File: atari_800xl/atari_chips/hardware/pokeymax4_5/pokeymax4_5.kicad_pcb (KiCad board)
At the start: 4 copper layers, 20.8 x 51.3 mm, 70 parts, among them J1 Conn_02x03_Odd_Even, J2 Conn_01x14_Pin, U2 TSV854IQ4T, U3 SN74CB3T16211DGVR, U5 SN74CB3T16211DGVR, Y1 ASE-49.152MHz

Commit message: Added pokeymax 4.54 (not yet made)
git-svn-id: svn+ssh://192.168.0.3/home/svnfpga/repo/trunk@1559 d6161ac3-aae1-4d52-9b05-ea9ac36b53d3
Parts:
- added C28: 220pF C0G, Capacitor_SMD:C_0402_1005Metric, F.Cu at (31.9, 30.6)
- added C29: 220pF C0G, Capacitor_SMD:C_0402_1005Metric, F.Cu at (25.6, 31.1)
- added R32: 31k6, Resistor_SMD:R_0402_1005Metric, F.Cu at (21.7, 29.3)
- added R33: 31k6, Resistor_SMD:R_0402_1005Metric, F.Cu at (30.6, 29.2)
- C13, C14: value 220pf C0G -> 220pF C0G
- R11, R13: value 560 -> 31k6
- R20, R21: value 33 -> 270
- moved C13 10.5 mm to (21.7, 28.3), turned to 180 degrees
- moved C14 4.54 mm to (29.6, 29.2), turned to 90 degrees
- moved R11 1.49 mm to (31.7, 29.2), turned to 90 degrees
- moved C9 0.94 mm to (32.5, 27.8)
- moved R12 0.63 mm to (32.7, 29.2), turned to 90 degrees
- moved R10 0.60 mm to (32.1, 26.8)
- moved C8 0.54 mm to (30.1, 27.8), turned to 180 degrees
- moved C10 0.53 mm to (23.7, 28.5), turned to 0 degrees
- moved R8 0.45 mm to (30.1, 26.8), turned to 180 degrees
- moved R14 0.40 mm to (30.0, 30.6)
- moved R15 0.26 mm to (21.9, 31.2)
- moved C12 0.21 mm to (21.7, 30.3)
- moved R16 0.19 mm to (23.7, 31.3)
- moved R13 0.06 mm to (23.6, 30.2), turned to 0 degrees
- moved C5 0.05 mm to (30.9, 24.9)
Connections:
- net Net-(J1-Pin_6) renamed /FPGA/TDO
- C12 pad 1: Net-(U2-IN2+) -> Net-(C12-Pad1)
- C13 pad 1: Net-(U2-OUT3) -> Net-(U2-IN2+)
- C13 pad 2: Net-(U2-IN3-) -> GND
- C14 pad 1: Net-(U2-OUT2) -> Net-(U2-IN3+)
- C14 pad 2: Net-(U2-IN2-) -> GND
- C9 pad 1: Net-(U2-IN3+) -> Net-(C9-Pad1)
- R11 pad 1: Net-(R11-Pad1) -> Net-(C9-Pad1)
- R11 pad 2: Net-(U2-IN3+) -> Net-(C28-Pad1)
- R13 pad 1: Net-(R13-Pad1) -> Net-(C12-Pad1)
- R13 pad 2: Net-(U2-IN2+) -> Net-(C29-Pad1)
- R20 pad 2: Net-(R13-Pad1) -> Net-(C12-Pad1)
- R21 pad 2: Net-(R11-Pad1) -> Net-(C9-Pad1)
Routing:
- net Net-(C9-Pad1): track 0.00 -> 20.4 mm, vias 0 -> 2
- net Net-(R11-Pad1): track 15.8 -> 0.00 mm, vias 2 -> 0
- net Net-(C12-Pad1): track 0.00 -> 12.6 mm, vias 0 -> 2
- net Net-(R13-Pad1): track 12.2 -> 0.00 mm, vias 2 -> 0
- net /Audio output/AUD_IN_AMP: track 52.4 -> 47.6 mm, vias 5 -> 3
- net Net-(C29-Pad1): track 0.00 -> 3.65 mm
- net Net-(C28-Pad1): track 0.00 -> 3.12 mm, vias 0 -> 2
- net Net-(U2-OUT3): track 14.0 -> 15.8 mm, vias 2 -> 0
- net Net-(U2-IN3+): track 4.14 -> 2.80 mm
- net Net-(U2-IN4-): track 5.90 -> 6.69 mm, vias 0 -> 2
- net Net-(U2-IN3-): track 6.11 -> 6.81 mm
- net Net-(U2-OUT2): track 20.5 -> 19.9 mm
- net Net-(U2-IN2-): track 5.28 -> 4.76 mm
- net +2V5: track 48.7 -> 49.2 mm
- net GND: track 63.2 -> 63.1 mm, vias 46 -> 45
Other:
- board text added: "Pokeymax 4.54"
- board text removed: "Pokeymax 4.53"

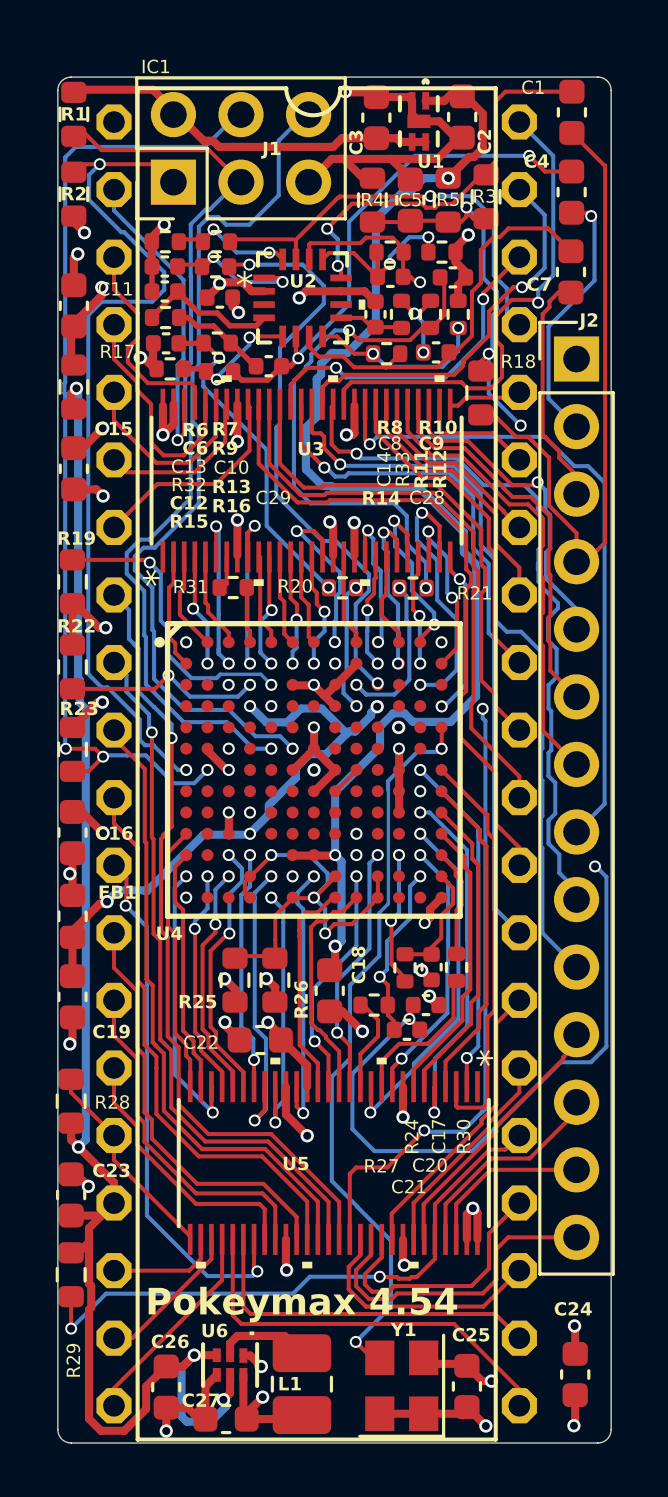
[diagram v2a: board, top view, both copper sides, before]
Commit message: 4.55. Got AI to help me improve a few minor things. Regulator mode, extra decoupling for DAC, distances from edge, gnd/power plane switched, track spacing for a few important lines, bigger cap on 2.5v reg, shorter critical traces on 3.3v reg. Also it double checked the sallen key filter. Switched to the JLCPCB plugin for simpler part management.
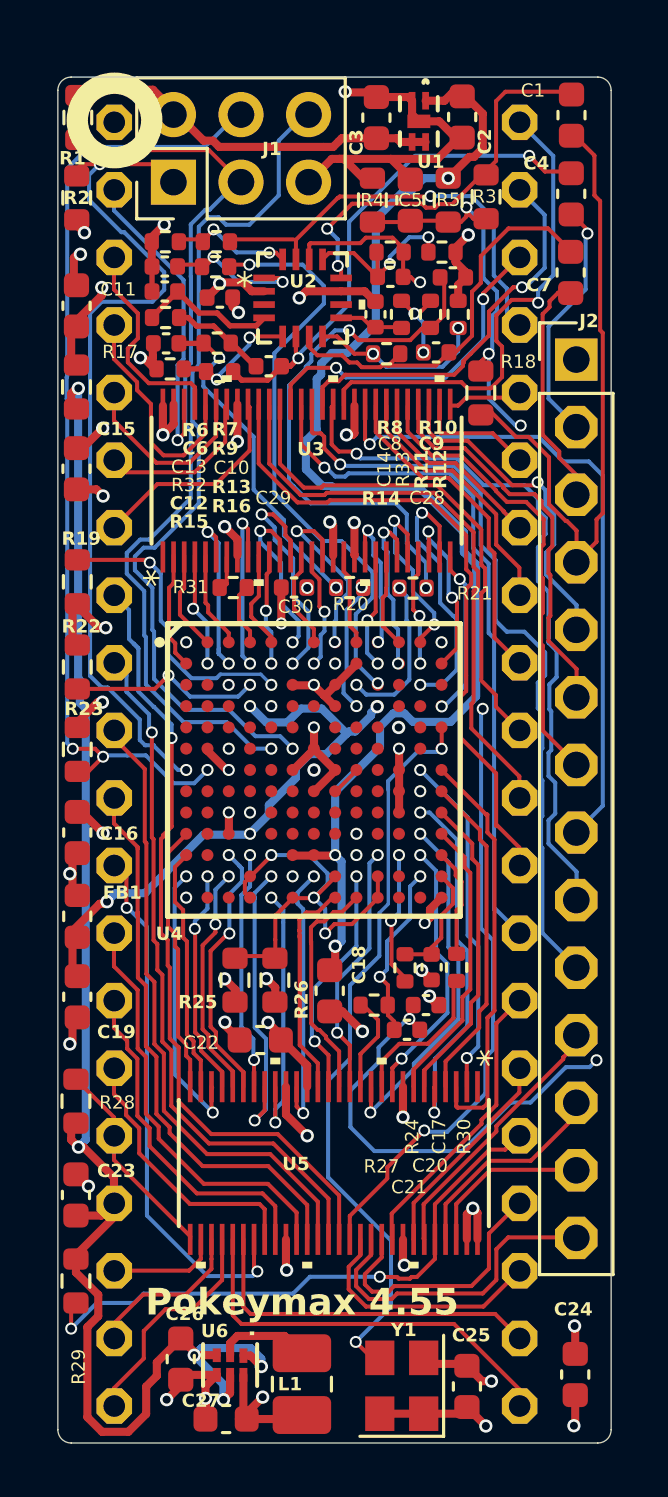
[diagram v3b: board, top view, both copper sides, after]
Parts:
- removed IC1: ~, ic-package:DIL40
- added C30: 0.1uF, Capacitor_SMD:C_0402_1005Metric, F.Cu at (26.5, 39.4)
- added J3: Conn_01x20_Pin, Connector_PinSocket_2.54mm:PinSocket_1x20_P2.54mm_Vertical, B.Cu at (35.0, 21.9)
- added J4: Conn_01x20_Pin, Connector_PinSocket_2.54mm:PinSocket_1x20_P2.54mm_Vertical, B.Cu at (19.8, 21.9)
- C1, C4, C7: value 2.2uF C0G -> 2.2uF C0G (4.7uF X7R alternative)
- C2: value 0.1uF -> 2u2
- C8: value 220pf C0G -> 220pF C0G
- R17: value 10 -> 33
- moved C26 1.19 mm to (22.3, 68.4)
- moved R29 0.30 mm to (18.3, 65.5)
- moved R20 0.27 mm to (28.6, 39.4)
- moved R1 0.19 mm to (18.4, 21.8)
- moved C16 0.18 mm to (18.4, 48.6)
- moved C19 0.18 mm to (18.4, 54.8)
- moved C23 0.18 mm to (18.3, 62.3)
- moved FB1 0.18 mm to (18.4, 51.8)
- moved R19 0.18 mm to (18.4, 39.2)
- moved R22 0.18 mm to (18.4, 42.4)
- moved R23 0.18 mm to (18.4, 45.5)
- moved R28 0.18 mm to (18.3, 58.8)
- moved R2 0.18 mm to (18.4, 24.8)
- moved C1 0.11 mm to (37.0, 21.7)
- moved C11 0.10 mm to (18.4, 28.9)
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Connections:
- U4 pad E1: unconnected-(U4-IO_UNUSED-PadE1)_24 -> /FPGA/unconnected-(U4-IO_UNUSED-PadE1)_1_24
- U4 pad E10: unconnected-(U4-IO_UNUSED-PadE1)_23 -> /FPGA/unconnected-(U4-IO_UNUSED-PadE1)_1_23
- U4 pad E12: unconnected-(U4-IO_UNUSED-PadE1)_1 -> /FPGA/unconnected-(U4-IO_UNUSED-PadE1)_1_1
- U4 pad E3: unconnected-(U4-IO_UNUSED-PadE1)_5 -> /FPGA/unconnected-(U4-IO_UNUSED-PadE1)_1_5
- U4 pad E4: unconnected-(U4-IO_UNUSED-PadE1)_6 -> /FPGA/unconnected-(U4-IO_UNUSED-PadE1)_1_6
- U4 pad E6: unconnected-(U4-IO_UNUSED-PadE1)_8 -> /FPGA/unconnected-(U4-IO_UNUSED-PadE1)_1_8
- U4 pad E8: unconnected-(U4-IO_UNUSED-PadE1)_26 -> /FPGA/unconnected-(U4-IO_UNUSED-PadE1)_1_26
- U4 pad E9: unconnected-(U4-IO_UNUSED-PadE1)_11 -> /FPGA/unconnected-(U4-IO_UNUSED-PadE1)_1_11
- U4 pad F1: unconnected-(U4-IO_UNUSED-PadE1)_4 -> /FPGA/unconnected-(U4-IO_UNUSED-PadE1)_1_4
- U4 pad F10: unconnected-(U4-IO_UNUSED-PadE1)_16 -> /FPGA/unconnected-(U4-IO_UNUSED-PadE1)_1_16
- U4 pad F12: unconnected-(U4-IO_UNUSED-PadE1)_22 -> /FPGA/unconnected-(U4-IO_UNUSED-PadE1)_1_22
- U4 pad F4: unconnected-(U4-IO_UNUSED-PadE1)_17 -> /FPGA/unconnected-(U4-IO_UNUSED-PadE1)_1_17
- U4 pad F8: unconnected-(U4-IO_UNUSED-PadE1)_9 -> /FPGA/unconnected-(U4-IO_UNUSED-PadE1)_1_9
- U4 pad F9: unconnected-(U4-IO_UNUSED-PadE1)_18 -> /FPGA/unconnected-(U4-IO_UNUSED-PadE1)_1_18
- U4 pad G10: unconnected-(U4-IO_UNUSED-PadE1)_12 -> /FPGA/unconnected-(U4-IO_UNUSED-PadE1)_1_12
- U4 pad G4: unconnected-(U4-IO_UNUSED-PadE1)_7 -> /FPGA/unconnected-(U4-IO_UNUSED-PadE1)_1_7
- U4 pad G5: unconnected-(U4-IO_UNUSED-PadE1)_2 -> /FPGA/unconnected-(U4-IO_UNUSED-PadE1)_1_2
- U4 pad H1: unconnected-(U4-IO_UNUSED-PadE1)_20 -> /FPGA/unconnected-(U4-IO_UNUSED-PadE1)_1_20
- U4 pad H10: unconnected-(U4-IO_UNUSED-PadE1)_25 -> /FPGA/unconnected-(U4-IO_UNUSED-PadE1)_1_25
- U4 pad H2: unconnected-(U4-IO_UNUSED-PadE1)_21 -> /FPGA/unconnected-(U4-IO_UNUSED-PadE1)_1_21
- U4 pad H3: unconnected-(U4-IO_UNUSED-PadE1)_15 -> /FPGA/unconnected-(U4-IO_UNUSED-PadE1)_1_15
- U4 pad H5: unconnected-(U4-IO_UNUSED-PadE1)_14 -> /FPGA/unconnected-(U4-IO_UNUSED-PadE1)_1_14
- U4 pad H9: unconnected-(U4-IO_UNUSED-PadE1)_19 -> /FPGA/unconnected-(U4-IO_UNUSED-PadE1)_1_19
- U4 pad J1: unconnected-(U4-IO_UNUSED-PadE1)_13 -> /FPGA/unconnected-(U4-IO_UNUSED-PadE1)_1_13
- U4 pad J10: unconnected-(U4-IO_UNUSED-PadE1) -> /FPGA/unconnected-(U4-IO_UNUSED-PadE1)_1
- U4 pad J2: unconnected-(U4-IO_UNUSED-PadE1)_10 -> /FPGA/unconnected-(U4-IO_UNUSED-PadE1)_1_10
- U4 pad J9: unconnected-(U4-IO_UNUSED-PadE1)_3 -> /FPGA/unconnected-(U4-IO_UNUSED-PadE1)_1_3
- U6 pad 1: GND -> +5V
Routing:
- net /FPGA/LIN1.A11: track 4.24 -> 8.90 mm
- net /FPGA/LIN1.A10: track 3.45 -> 6.43 mm, vias 0 -> 2
- net +5V: track 57.3 -> 59.3 mm, vias 4 -> 5
- net GND: track 63.1 -> 64.3 mm, vias 45 -> 46
- net /Audio output/AUD_IN_AMP: track 47.6 -> 46.7 mm
- net /Audio output/AUDLOUT: track 9.91 -> 9.29 mm
- net /Level shifter/LOUT2.B21: track 7.94 -> 8.54 mm
- net /Level shifter/LOUT2.B22: track 5.64 -> 6.18 mm
- net /FPGA/TCK: track 37.1 -> 36.6 mm
- net +3.3V: vias 15 -> 16
- added copper zone on In2.Cu, net +3.3V
- added copper zone on In1.Cu, net GND
- removed copper zone on In1.Cu, net +3.3V
- removed copper zone on In2.Cu, net GND
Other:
- board text added: "Pokeymax 4.55"
- board text removed: "Pokeymax 4.54"

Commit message: Tried to give me space between ADC and S/PDIF traces
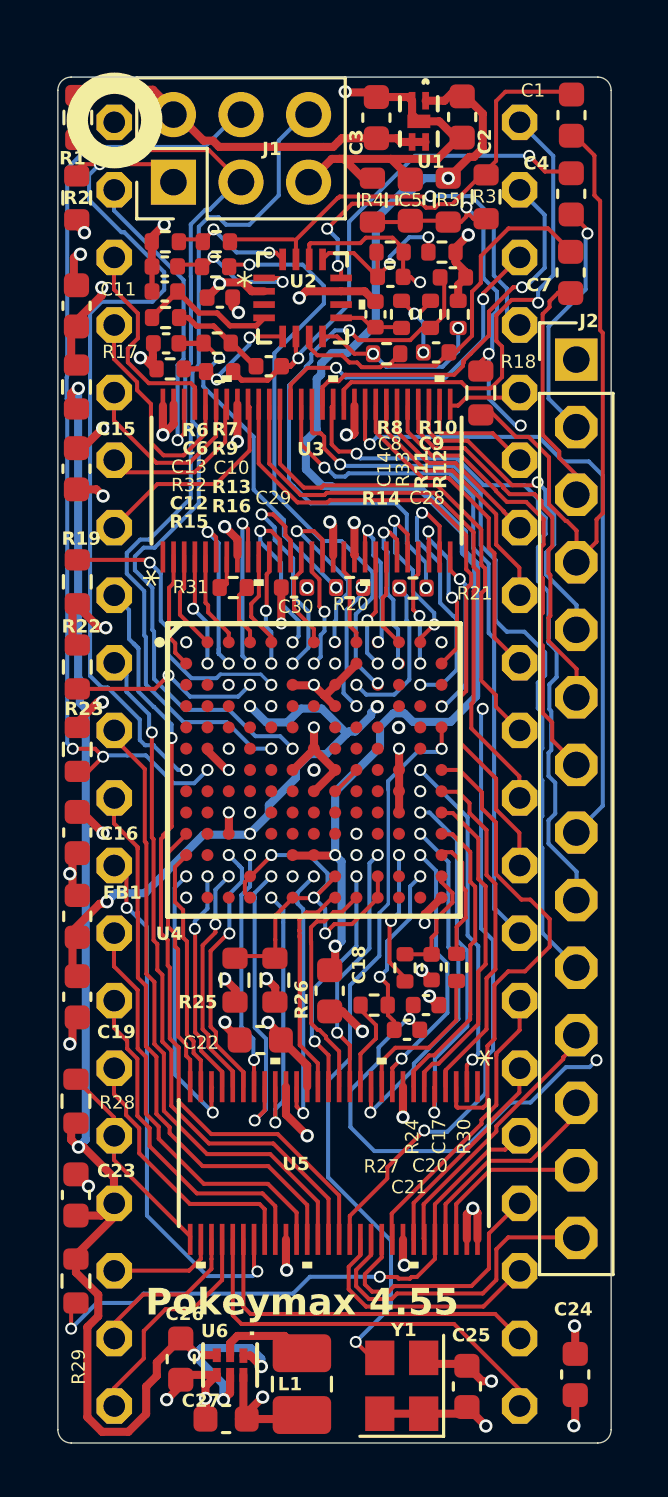
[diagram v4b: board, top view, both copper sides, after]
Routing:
- net /FPGA/LIN2.A2: track 15.5 -> 18.1 mm
- net /FPGA/LIN2.A3: track 12.4 -> 13.1 mm
- net /FPGA/LIN2.A5: track 11.7 -> 12.3 mm
- net Net-(U4-BB$19): track 4.08 -> 4.61 mm
- net /FPGA/LIN2.A6: track 10.8 -> 11.3 mm
